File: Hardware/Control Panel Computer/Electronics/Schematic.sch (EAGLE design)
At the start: 20 parts, among them IC1 7805T, J1 1X2-3.5MM, J2 1X2-3.5MM, J3 1X2-3.5MM, J4 1X2-3.5MM, J5 1X2-3.5MM

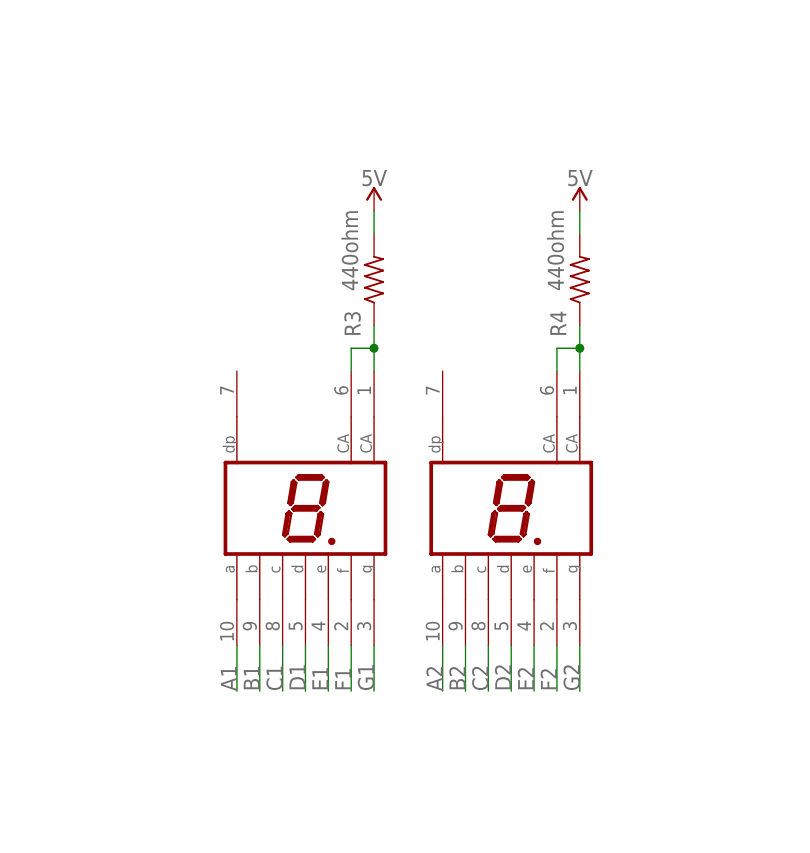
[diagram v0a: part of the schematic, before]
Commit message: remove 7-seg displays and complete board design
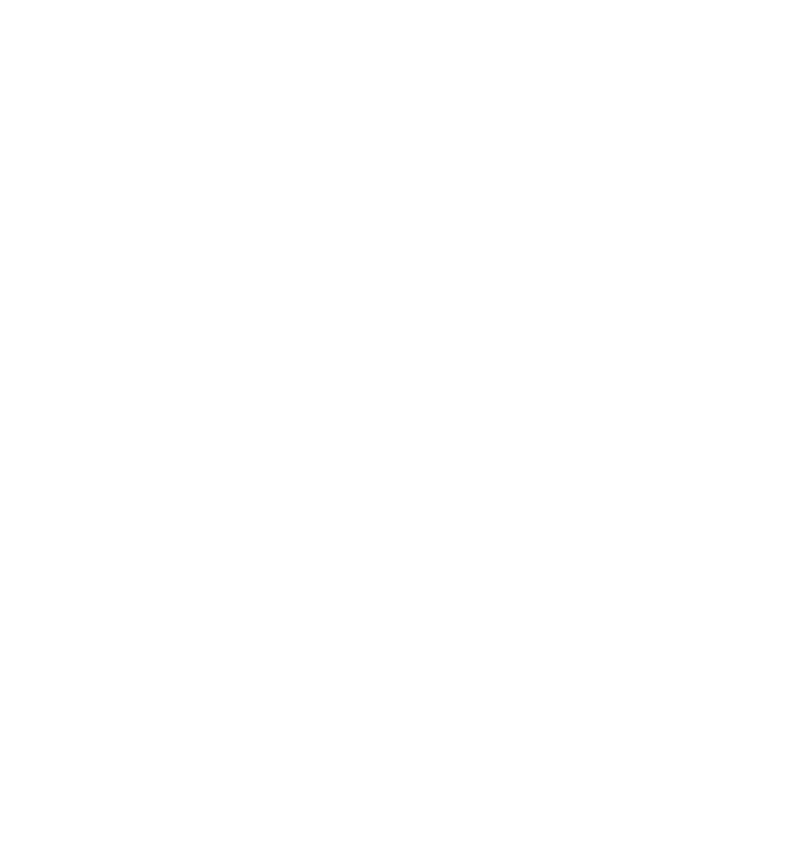
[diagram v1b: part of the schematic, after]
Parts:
- removed DIS2, DIS3: HD-A101, display-hp:HD-A101
- removed R3, R4: 440ohm, adafruit:R-US_0204/5
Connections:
- removed net N$1: DIS2.CA, DIS2.CA@1, R3.1
- removed net N$2: DIS3.CA, DIS3.CA@1, R4.1
- net 5V: no longer R3.2, R4.2
- net A1: no longer DIS2.A
- net A2: no longer DIS3.A
- net B1: no longer DIS2.B
- net B2: no longer DIS3.B
- net C1: no longer DIS2.C
- net C2: no longer DIS3.C
- net D1: no longer DIS2.D
- net D2: no longer DIS3.D
- net E1: no longer DIS2.E
- net E2: no longer DIS3.E
- net F1: no longer DIS2.F
- net F2: no longer DIS3.F
- net G1: no longer DIS2.G
- net G2: no longer DIS3.G

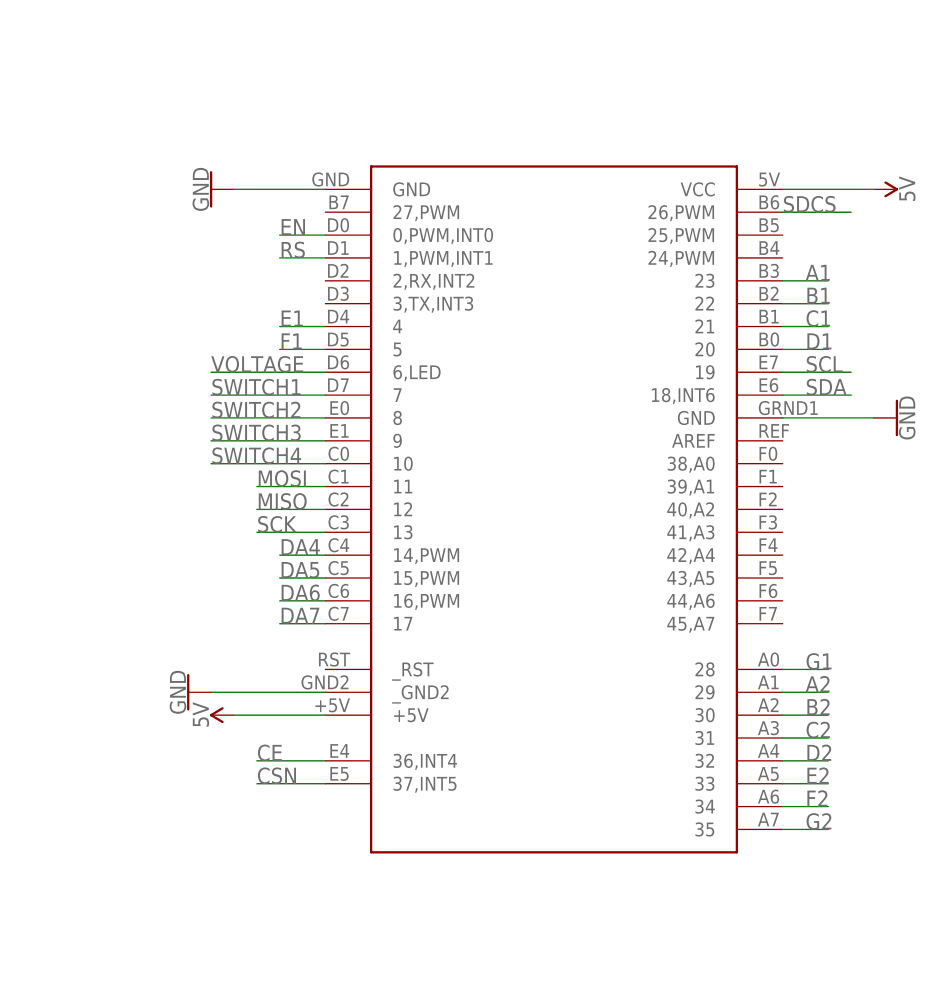
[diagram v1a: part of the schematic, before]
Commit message: change control panel processor to STM32 Bluepill
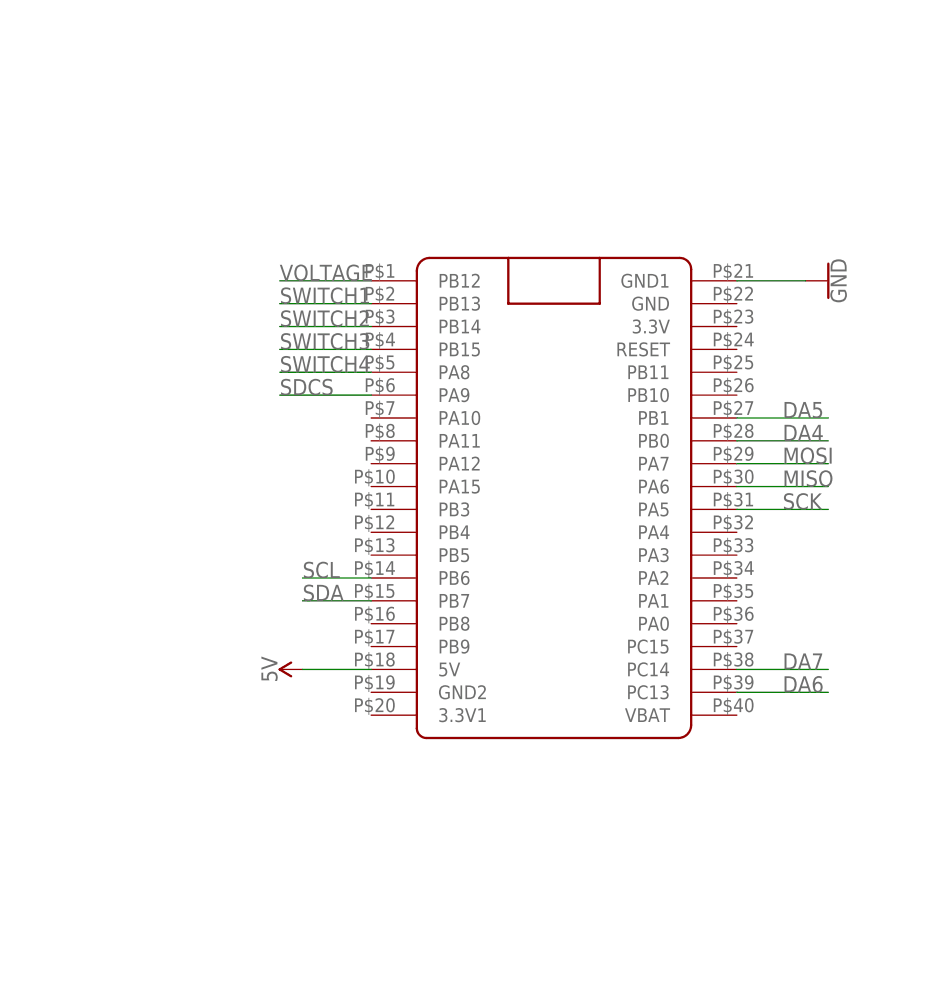
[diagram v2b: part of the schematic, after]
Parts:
- removed U$5: ARDUINO-TEENSY++, teensypp:ARDUINO-TEENSY++
- added U$6: (no value), BluePill:BLUE_PILL
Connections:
- removed net A1: U$5.23
- removed net A2: U$5.29
- removed net B1: U$5.22
- removed net B2: U$5.30
- removed net C1: U$5.21
- removed net C2: U$5.31
- removed net D1: U$5.20
- removed net D2: U$5.32
- removed net E1: U$5.4
- removed net E2: U$5.33
- removed net F1: U$5.5
- removed net F2: U$5.34
- removed net G1: U$5.28
- removed net G2: U$5.35
- net 5V: now also U$6.5V; no longer U$5.+5V, U$5.VCC
- net CE: no longer U$5.36,INT4
- net CSN: no longer U$5.37,INT5
- net DA4: now also U$6.PB0; no longer U$5.14,PWM
- net DA5: now also U$6.PB1; no longer U$5.15,PWM
- net DA6: now also U$6.PC13; no longer U$5.16,PWM
- net DA7: now also U$6.PC14; no longer U$5.17
- net EN: no longer U$5.0,PWM,INT0
- net GND: now also U$6.GND1; no longer U$5.GND, U$5.GND@1, U$5._GND2
- net MISO: now also U$6.PA6; no longer U$5.12
- net MOSI: now also U$6.PA7; no longer U$5.11
- net RS: no longer U$5.1,PWM,INT1
- net SCK: now also U$6.PA5; no longer U$5.13
- net SCL: now also U$6.PB6; no longer U$5.19
- net SDA: now also U$6.PB7; no longer U$5.18,INT6
- net SDCS: now also U$6.PA9; no longer U$5.26,PWM
- net SWITCH1: now also U$6.PB13; no longer U$5.7
- net SWITCH2: now also U$6.PB14; no longer U$5.8
- net SWITCH3: now also U$6.PB15; no longer U$5.9
- net SWITCH4: now also U$6.PA8; no longer U$5.10
- net VOLTAGE: now also U$6.PB12; no longer U$5.6,LED
